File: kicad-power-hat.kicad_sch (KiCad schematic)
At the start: 29 parts, among them J1 Raspberry_Pi_2_3, J2 AC Power In, J3 Screw_Terminal_01x03, Q1 BC847, Q2 BC857, Q3 BC857, U1 SP3485EEN, U2 LM2596S-5

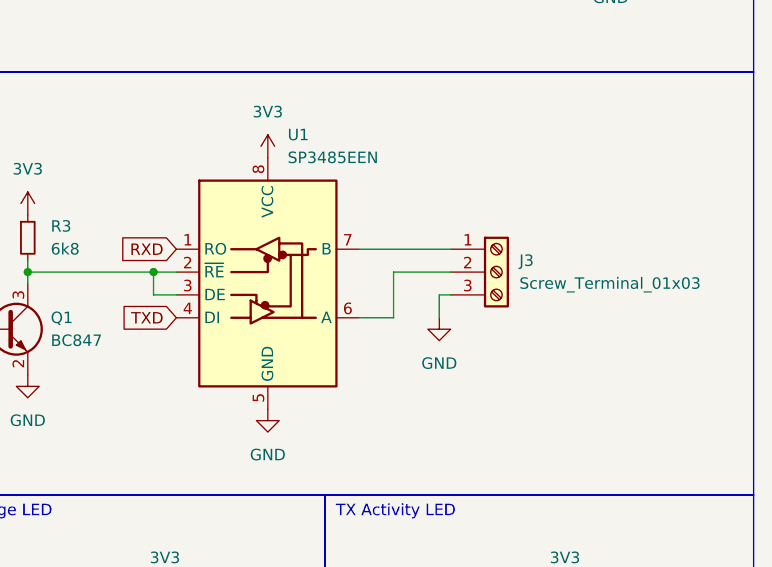
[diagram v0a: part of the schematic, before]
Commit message: wip: update to layout and labels
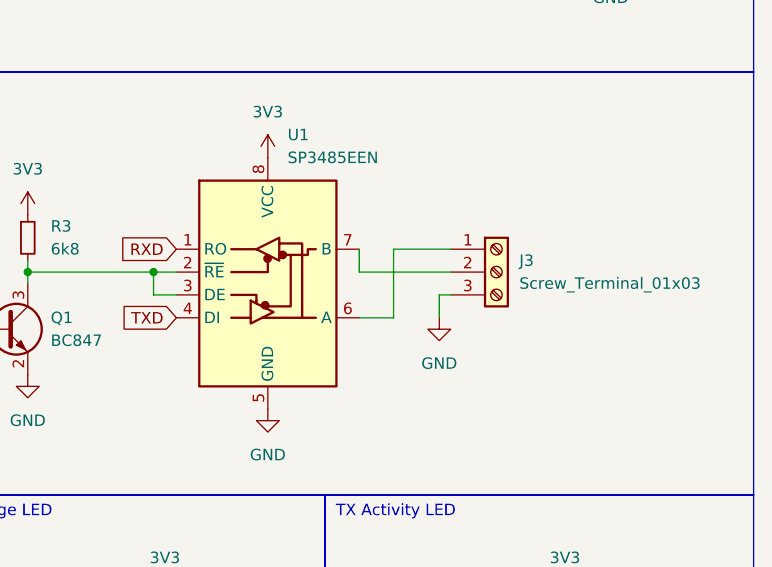
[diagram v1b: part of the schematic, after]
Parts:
- J3: footprint TerminalBlock_Phoenix:TerminalBlock_Phoenix_MPT-0,5-3-2.54_1x03_P2.54mm_Horizontal -> TerminalBlock_Phoenix:TerminalBlock_Phoenix_MKDS-1,5-3-5.08_1x03_P5.08mm_Horizontal
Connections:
- net at J3.1 (Pin_1): now also U1.6 (A); no longer U1.7 (B)
- net at J3.2 (Pin_2): now also U1.7 (B); no longer U1.6 (A)
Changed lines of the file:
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@@
+	(wire
+		(pts
+			(xy 238.76 85.09) (xy 238.76 87.63)
+		)
+		(stroke
+			(width 0)
+			(type default)
+		)
+	)
 	(wire
 		(pts
@@
 	(wire
 		(pts
-			(xy 238.76 85.09) (xy 248.92 85.09)
-		)
-		(stroke
-			(width 0)
-			(type default)
-		)
-	)
-	(wire
-		(pts
 			(xy 266.7 39.37) (xy 266.7 43.18)
 		)
@@
 	(wire
 		(pts
+			(xy 238.76 87.63) (xy 248.92 87.63)
+		)
+		(stroke
+			(width 0)
+			(type default)
+		)
+	)
+	(wire
+		(pts
 			(xy 173.99 48.26) (xy 173.99 54.61)
 		)
@@
 	(wire
 		(pts
+			(xy 242.57 85.09) (xy 248.92 85.09)
+		)
+		(stroke
+			(width 0)
+			(type default)
+		)
+	)
+	(wire
+		(pts
 			(xy 252.73 39.37) (xy 257.81 39.37)
 		)
@@
 	(wire
 		(pts
-			(xy 242.57 87.63) (xy 248.92 87.63)
-		)
-		(stroke
-			(width 0)
-			(type default)
-		)
-	)
-	(wire
-		(pts
 			(xy 201.93 86.36) (xy 201.93 87.63)
 		)
@@
 	(wire
 		(pts
-			(xy 242.57 92.71) (xy 242.57 87.63)
+			(xy 242.57 85.09) (xy 242.57 92.71)
 		)
 		(stroke
@@
 			)
 		)
-		(property "Footprint" "TerminalBlock_Phoenix:TerminalBlock_Phoenix_MPT-0,5-3-2.54_1x03_P2.54mm_Horizontal"
+		(property "Footprint" "TerminalBlock_Phoenix:TerminalBlock_Phoenix_MKDS-1,5-3-5.08_1x03_P5.08mm_Horizontal"
 			(at 254 87.63 0)
 			(effects

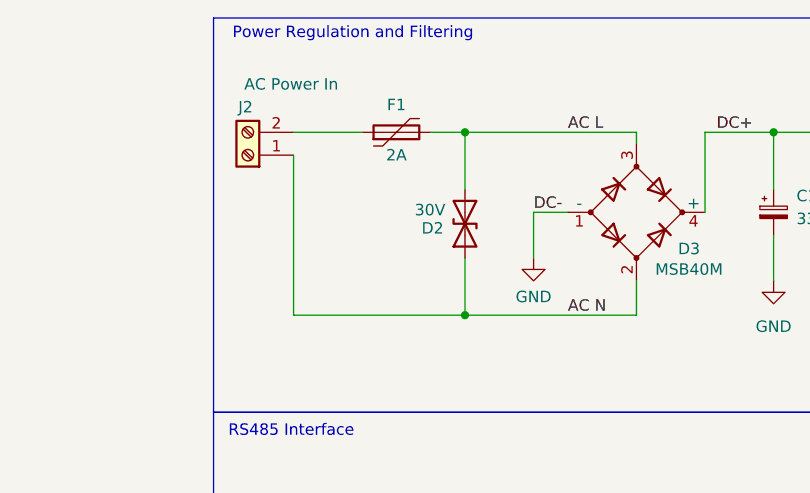
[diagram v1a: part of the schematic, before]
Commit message: wip: update to layout and labels
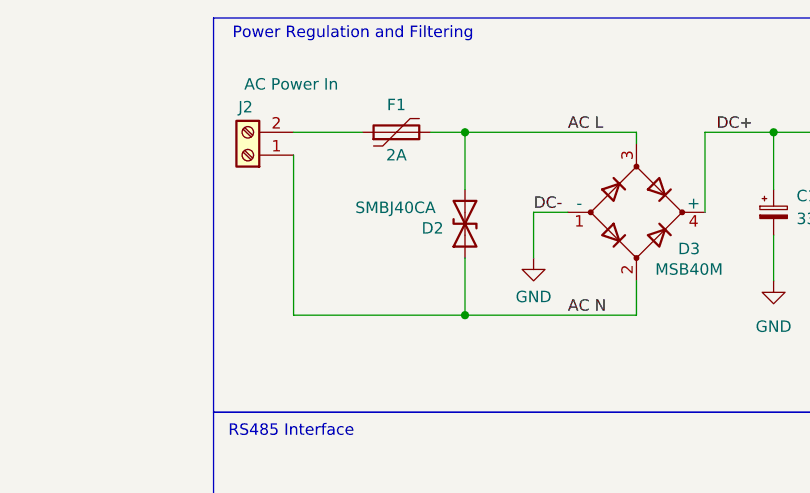
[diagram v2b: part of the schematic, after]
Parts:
- D2: value 30V -> SMBJ40CA; CODE SMBJ30CA -> SMBJ40CA; LCSC C353367 -> C84730
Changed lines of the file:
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@@
 	(title_block
 		(title "Raspberry 485 Power Hat")
-		(date "2024-03-02")
+		(date "2024-03-03")
 		(rev "2.0")
 		(company "Provvedo LLC")
@@
 			)
 		)
-		(property "Value" "30V"
-			(at 168.402 42.926 90)
+		(property "Value" "SMBJ40CA"
+			(at 161.798 42.672 90)
 			(effects
 				(font
@@
 			)
 		)
-		(property "CODE" "SMBJ30CA"
+		(property "CODE" "SMBJ40CA"
 			(at 173.99 44.45 90)
 			(effects
@@
 			)
 		)
-		(property "LCSC" "C353367"
+		(property "LCSC" "C84730"
 			(at 173.99 44.45 90)
 			(effects

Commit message: Updated pcb
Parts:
- added C3: 1u, Capacitor_SMD:C_0805_2012Metric, symbol Device:C_Small
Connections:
- net 3V3: now also C3.1
- net GND: now also C3.2
- net RS485-A: now reaches J3.1 (Pin_1), U1.6 (A)
- net RS485-B: now reaches J3.2 (Pin_2), U1.7 (B)
- no-connect marks 0 -> 25
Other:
- moved on the sheet: J3

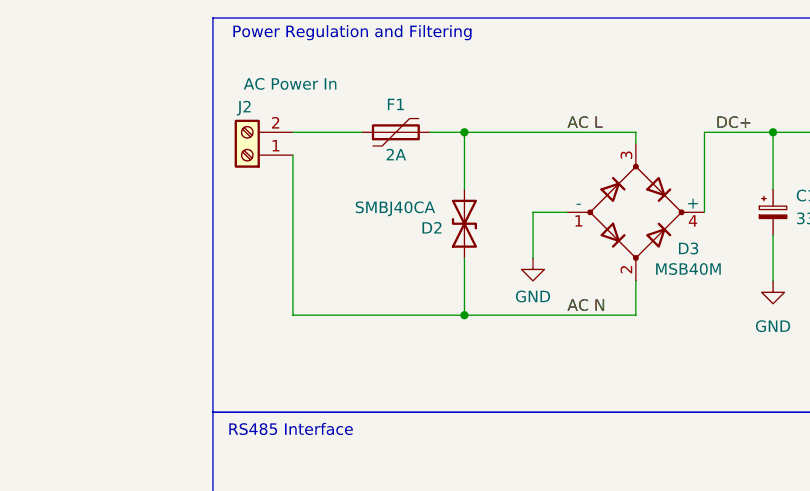
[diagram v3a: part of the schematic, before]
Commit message: fix: cleanup backups and update crowbar diode part number
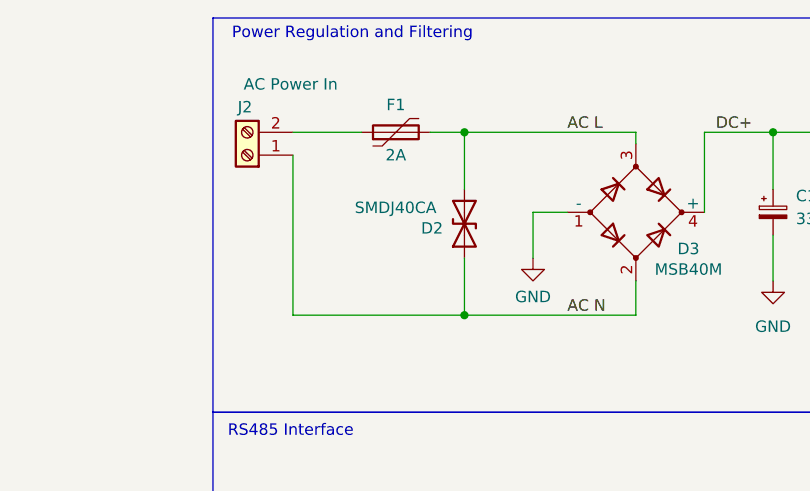
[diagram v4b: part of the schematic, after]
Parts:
- D2: value SMBJ40CA -> SMDJ40CA
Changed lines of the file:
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@@
 			)
 		)
-		(property "Value" "SMBJ40CA"
+		(property "Value" "SMDJ40CA"
 			(at 161.798 42.672 90)
 			(effects

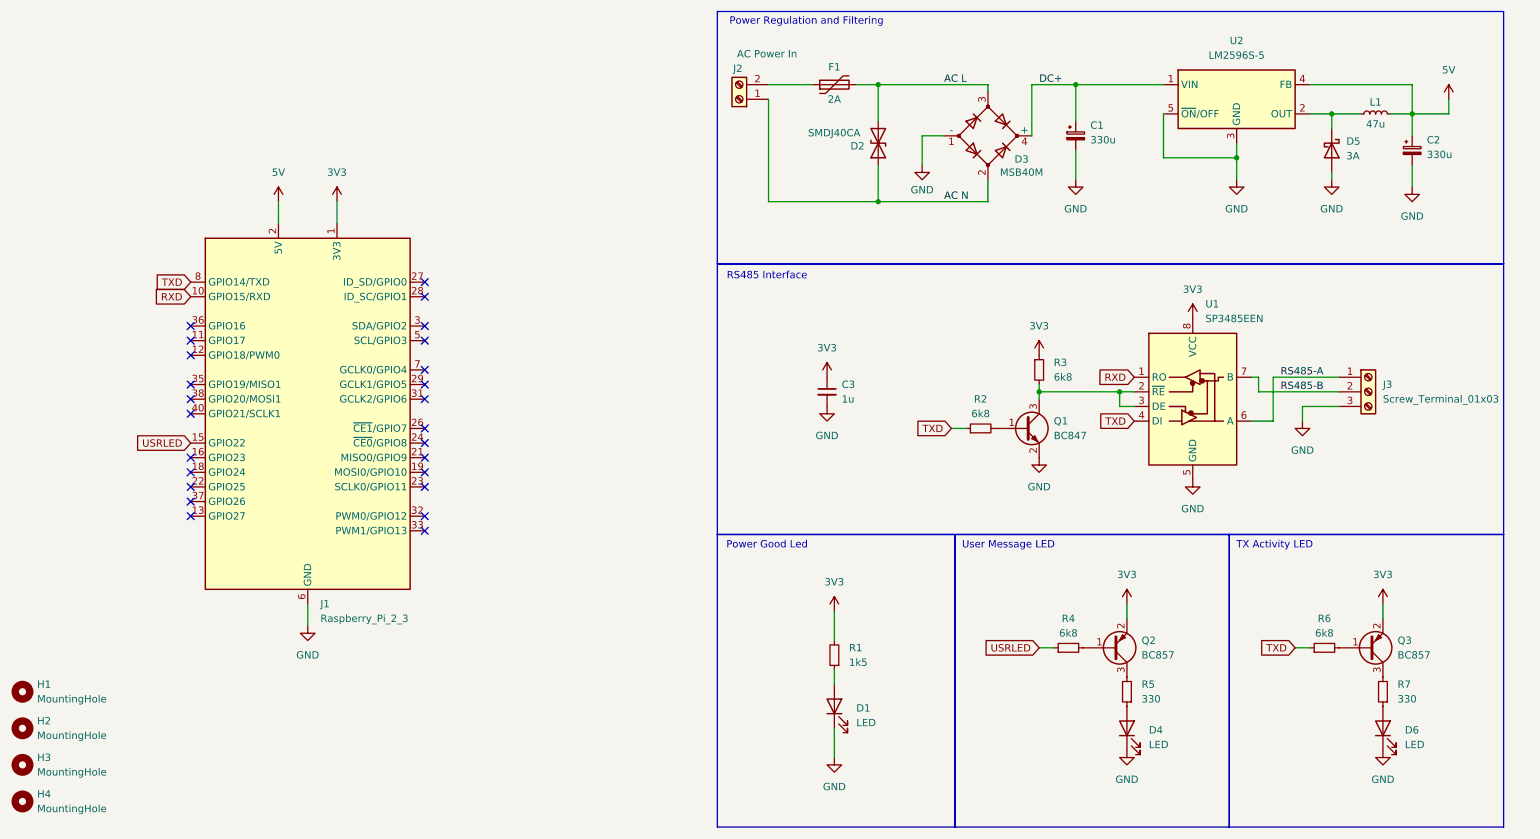
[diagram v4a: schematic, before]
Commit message: fix: Update holes pattern and footprint for rectifier
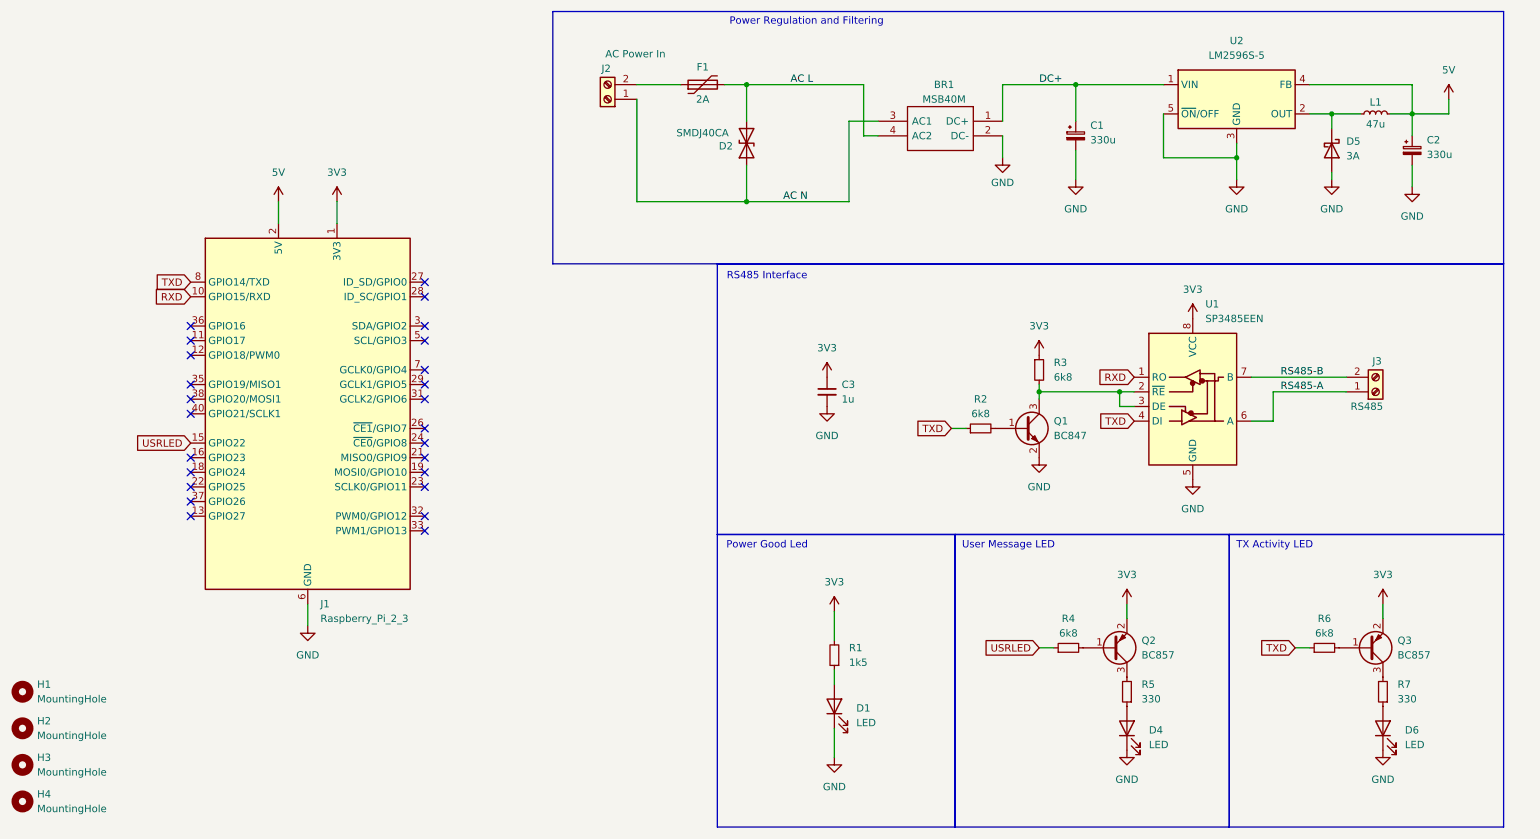
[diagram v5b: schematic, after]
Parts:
- removed D3: MSB40M, Diode_SMD:Diode_Bridge_Bourns_CD-DF4xxS, symbol Device:D_Bridge_+A-A
- removed J3: Screw_Terminal_01x03, TerminalBlock_Phoenix:TerminalBlock_Phoenix_MKDS-1,5-3-5.08_1x03_P5.08mm_Horizontal, symbol Connector:Screw_Terminal_01x03
- added BR1: MSB40M, SOTFL510P865X150-4N, symbol SamacSys_Parts:MSB40M
- added J3: RS485, TerminalBlock_Phoenix:TerminalBlock_Phoenix_MKDS-1,5-2-5.08_1x02_P5.08mm_Horizontal, symbol Connector:Screw_Terminal_01x02
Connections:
- net AC L: now also BR1.4 (AC2)
- net AC N: now also BR1.3 (AC1)
- net DC+: now also BR1.1 (DC+)
- net GND: now also BR1.2 (DC-)
- net RS485-A: now also J3.1 (Pin_1)
- net RS485-B: now also J3.2 (Pin_2)
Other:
- moved on the sheet: D2, F1, J2
